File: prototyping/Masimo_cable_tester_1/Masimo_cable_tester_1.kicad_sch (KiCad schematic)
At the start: 28 parts, among them J1 Touchscreen HMI, J10 5V Jumper, J16 Debug Connections, J17 Banana Jack, J2 Conn_01x28_Socket, J3 Conn_01x28_Socket, J4 Barrel Jack 9V, J5 Conn_01x08, J6 SFML-110-02-L-D-A, J7 Conn_01x03_Pin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

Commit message: Prototype Schematic and PCB Updates
Made a few changes to the schematic for ease of tracing on the PCB design. Started PCB layout of components, no traces yet
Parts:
- J10: value 5V Jumper -> MCU Board Power
- J2: value Conn_01x28_Socket -> Curiosity Nano AVR128DB48
- J5: value Conn_01x08 -> MicroSD PinHeader
- J7: value Conn_01x03_Pin -> HMI Power Toggle
- J8: value Jumper Pins 5V -> Board Power
- J9: value VOFF Jumper -> VOFF Toggle
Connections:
- net ADC 1: now also J6.02; no longer J6.01
- net ADC 10: now also J6.20; no longer J6.10
- net ADC 2: now also J6.04; no longer J6.03
- net ADC 3: now also J6.06; no longer J6.05
- net ADC 4: now also J6.08; no longer J6.07
- net ADC 5: now also J6.10; no longer J6.09
- net ADC 6: now also J6.12; no longer J6.02
- net ADC 7: now also J6.14; no longer J6.04
- net ADC 8: now also J6.16; no longer J6.06
- net ADC 9: now also J6.18; no longer J6.08
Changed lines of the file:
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@@
 	(global_label "MP10"
 		(shape input)
-		(at 166.37 92.71 0)
+		(at 166.37 105.41 0)
 		(fields_autoplaced yes)
 		(effects
@@
 		)
 		(property "Intersheetrefs" "${INTERSHEET_REFS}"
-			(at 174.4956 92.71 0)
+			(at 174.4956 105.41 0)
 			(effects
 				(font
@@
 	(global_label "MP3"
 		(shape input)
-		(at 140.97 87.63 180)
+		(at 166.37 87.63 0)
 		(fields_autoplaced yes)
 		(effects
@@
 				(size 1.27 1.27)
 			)
-			(justify right)
+			(justify left)
 		)
 		(property "Intersheetrefs" "${INTERSHEET_REFS}"
-			(at 134.0539 87.63 0)
+			(at 173.2861 87.63 0)
 			(effects
 				(font
 					(size 1.27 1.27)
 				)
-				(justify right)
+				(justify left)
 				(hide yes)
 			)
@@
 	(global_label "MP7"
 		(shape input)
-		(at 166.37 85.09 0)
+		(at 166.37 97.79 0)
 		(fields_autoplaced yes)
 		(effects
@@
 		)
 		(property "Intersheetrefs" "${INTERSHEET_REFS}"
-			(at 173.2861 85.09 0)
+			(at 173.2861 97.79 0)
 			(effects
 				(font
@@
 	(global_label "MP4"
 		(shape input)
-		(at 140.97 90.17 180)
+		(at 166.37 90.17 0)
 		(fields_autoplaced yes)
 		(effects
@@
 				(size 1.27 1.27)
 			)
-			(justify right)
+			(justify left)
 		)
 		(property "Intersheetrefs" "${INTERSHEET_REFS}"
-			(at 134.0539 90.17 0)
+			(at 173.2861 90.17 0)
 			(effects
 				(font
 					(size 1.27 1.27)
 				)
-				(justify right)
+				(justify left)
 				(hide yes)
 			)
@@
 	(global_label "MP5"
 		(shape input)
-		(at 140.97 92.71 180)
+		(at 166.37 92.71 0)
 		(fields_autoplaced yes)
 		(effects
@@
 				(size 1.27 1.27)
 			)
-			(justify right)
+			(justify left)
 		)
 		(property "Intersheetrefs" "${INTERSHEET_REFS}"
-			(at 134.0539 92.71 0)
+			(at 173.2861 92.71 0)
 			(effects
 				(font
 					(size 1.27 1.27)
 				)
-				(justify right)
+				(justify left)
 				(hide yes)
 			)
@@
 	(global_label "MP6"
 		(shape input)
-		(at 166.37 82.55 0)
+		(at 166.37 95.25 0)
 		(fields_autoplaced yes)
 		(effects
@@
 		)
 		(property "Intersheetrefs" "${INTERSHEET_REFS}"
-			(at 173.2861 82.55 0)
+			(at 173.2861 95.25 0)
 			(effects
 				(font
@@
 	(global_label "MP2"
 		(shape input)
-		(at 140.97 85.09 180)
+		(at 166.37 85.09 0)
 		(fields_autoplaced yes)
 		(effects
@@
 				(size 1.27 1.27)
 			)
-			(justify right)
+			(justify left)
 		)
 		(property "Intersheetrefs" "${INTERSHEET_REFS}"
-			(at 134.0539 85.09 0)
+			(at 173.2861 85.09 0)
 			(effects
 				(font
 					(size 1.27 1.27)
 				)
-				(justify right)
+				(justify left)
 				(hide yes)
 			)
@@
 	(global_label "MP9"
 		(shape input)
-		(at 166.37 90.17 0)
+		(at 166.37 102.87 0)
 		(fields_autoplaced yes)
 		(effects
@@
 		)
 		(property "Intersheetrefs" "${INTERSHEET_REFS}"
-			(at 173.2861 90.17 0)
+			(at 173.2861 102.87 0)
 			(effects
 				(font
@@
 	(global_label "MP8"
 		(shape input)
-		(at 166.37 87.63 0)
+		(at 166.37 100.33 0)
 		(fields_autoplaced yes)
 		(effects
@@
 		)
 		(property "Intersheetrefs" "${INTERSHEET_REFS}"
-			(at 173.2861 87.63 0)
+			(at 173.2861 100.33 0)
 			(effects
 				(font
@@
 	(global_label "MP1"
 		(shape input)
-		(at 140.97 82.55 180)
+		(at 166.37 82.55 0)
 		(fields_autoplaced yes)
 		(effects
@@
 				(size 1.27 1.27)
 			)
-			(justify right)
+			(justify left)
 		)
 		(property "Intersheetrefs" "${INTERSHEET_REFS}"
-			(at 134.0539 82.55 0)
+			(at 173.2861 82.55 0)
 			(effects
 				(font
 					(size 1.27 1.27)
 				)
-				(justify right)
+				(justify left)
 				(hide yes)
 			)
@@
 		(dnp no)
 		(property "Reference" "C2"
-			(at 93.98 43.1799 0)
+			(at 90.678 42.418 0)
 			(effects
 				(font
@@
 				)
 				(justify left)
-				(hide yes)
 			)
 		)
@@
 		(on_board yes)
 		(dnp no)
-		(fields_autoplaced yes)
 		(property "Reference" "J8"
 			(at 102.87 34.9249 90)
@@
 			)
 		)
-		(property "Value" "Jumper Pins 5V"
-			(at 102.87 37.4649 90)
+		(property "Value" "Board Power"
+			(at 94.488 33.782 90)
 			(effects
 				(font
@@
 		(dnp no)
 		(property "Reference" "C1"
-			(at 67.31 43.1799 0)
+			(at 70.866 42.164 0)
 			(effects
 				(font
@@
 				)
 				(justify left)
-				(hide yes)
 			)
 		)
@@
 			)
 		)
-		(property "Value" "Conn_01x08"
+		(property "Value" "MicroSD PinHeader"
 			(at 139.7 33.02 0)
 			(effects
@@
 		(on_board yes)
 		(dnp no)
-		(fields_autoplaced yes)
 		(property "Reference" "J9"
 			(at 91.44 114.9349 90)
@@
 			)
 		)
-		(property "Value" "VOFF Jumper"
-			(at 91.44 117.4749 90)
+		(property "Value" "VOFF Toggle"
+			(at 83.566 113.792 90)
 			(effects
 				(font
@@
 			)
 		)
-		(property "Value" "Conn_01x03_Pin"
+		(property "Value" "HMI Power Toggle"
 			(at 78.74 86.3599 0)
 			(effects
@@
 		(on_board yes)
 		(dnp no)
-		(fields_autoplaced yes)
 		(property "Reference" "J10"
 			(at 86.36 136.5251 90)
@@
 			)
 		)
-		(property "Value" "5V Jumper"
-			(at 91.44 135.2549 90)
+		(property "Value" "MCU Board Power"
+			(at 81.026 137.668 90)
 			(effects
 				(font
@@
 			)
 		)
-		(property "Value" "Conn_01x28_Socket"
+		(property "Value" "Curiosity Nano AVR128DB48"
 			(at 49.53 153.6699 0)
 			(effects

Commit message: Layed traces down.
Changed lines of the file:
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@@
 (kicad_sch
-	(version 20231120)
+	(version 20250114)
 	(generator "eeschema")
-	(generator_version "8.0")
+	(generator_version "9.0")
 	(paper "A")
 	(title_block
@@
 		(comment 1 "Designed for use with the AVR128DB48 Curiosity Nano")
 	)
+	(rectangle
+		(start 19.05 24.765)
+		(end 121.285 60.325)
+		(stroke
+			(width 0)
+			(type default)
+		)
+		(fill
+			(type none)
+		)
+	)
+	(rectangle
+		(start 193.04 45.085)
+		(end 255.905 154.305)
+		(stroke
+			(width 0)
+			(type default)
+		)
+		(fill
+			(type none)
+		)
+	)
+	(text "Signal Relay"
+		(exclude_from_sim no)
+		(at 146.05 129.286 0)
+		(effects
+			(font
+				(size 2.032 2.032)
+				(thickness 0.4064)
+				(bold yes)
+			)
+		)
+	)
+	(text "MicroSD"
+		(exclude_from_sim no)
+		(at 144.272 26.924 0)
+		(effects
+			(font
+				(size 2.032 2.032)
+				(thickness 0.4064)
+				(bold yes)
+			)
+		)
+	)
+	(text "20-Pin Connector"
+		(exclude_from_sim no)
+		(at 153.416 73.914 0)
+		(effects
+			(font
+				(size 2.032 2.032)
+				(thickness 0.4064)
+				(bold yes)
+			)
+		)
+	)
+	(text "Power"
+		(exclude_from_sim no)
+		(at 65.024 30.226 0)
+		(effects
+			(font
+				(size 2.032 2.032)
+				(thickness 0.4064)
+				(bold yes)
+			)
+		)
+	)
+	(text "AVR128DB48\nMicrocontroller"
+		(exclude_from_sim no)
+		(at 54.356 109.22 0)
+		(effects
+			(font
+				(size 2.54 2.54)
+				(thickness 0.508)
+				(bold yes)
+			)
+		)
+	)
+	(text "Analog IF"
+		(exclude_from_sim no)
+		(at 225.044 49.276 0)
+		(effects
+			(font
+				(size 2.032 2.032)
+				(thickness 0.4064)
+				(bold yes)
+			)
+		)
+	)
 	(junction
 		(at 227.33 69.85)
@@
 		)
 	)
-	(rectangle
-		(start 19.05 24.765)
-		(end 121.285 60.325)
-		(stroke
-			(width 0)
-			(type default)
-		)
-		(fill
-			(type none)
-		)
-	)
-	(rectangle
-		(start 193.04 45.085)
-		(end 255.905 154.305)
-		(stroke
-			(width 0)
-			(type default)
-		)
-		(fill
-			(type none)
-		)
-	)
-	(text "Signal Relay"
-		(exclude_from_sim no)
-		(at 146.05 129.286 0)
-		(effects
-			(font
-				(size 2.032 2.032)
-				(thickness 0.4064)
-				(bold yes)
-			)
-		)
-	)
-	(text "MicroSD"
-		(exclude_from_sim no)
-		(at 144.272 26.924 0)
-		(effects
-			(font
-				(size 2.032 2.032)
-				(thickness 0.4064)
-				(bold yes)
-			)
-		)
-	)
-	(text "20-Pin Connector"
-		(exclude_from_sim no)
-		(at 153.416 73.914 0)
-		(effects
-			(font
-				(size 2.032 2.032)
-				(thickness 0.4064)
-				(bold yes)
-			)
-		)
-	)
-	(text "Power"
-		(exclude_from_sim no)
-		(at 65.024 30.226 0)
-		(effects
-			(font
-				(size 2.032 2.032)
-				(thickness 0.4064)
-				(bold yes)
-			)
-		)
-	)
-	(text "AVR128DB48\nMicrocontroller"
-		(exclude_from_sim no)
-		(at 54.356 109.22 0)
-		(effects
-			(font
-				(size 2.54 2.54)
-				(thickness 0.508)
-				(bold yes)
-			)
-		)
-	)
-	(text "Analog IF"
-		(exclude_from_sim no)
-		(at 225.044 49.276 0)
-		(effects
-			(font
-				(size 2.032 2.032)
-				(thickness 0.4064)
-				(bold yes)
-			)
-		)
-	)
 	(global_label "5V"
 		(shape input)
@@
 		)
 	)
+	(embedded_fonts no)
 )

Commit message: PCB Update
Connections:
- net ADC 1: now also J3.12 (Pin_12); no longer J3.22 (Pin_22)
- net ADC 10: now also J3.22 (Pin_22); no longer J3.10 (Pin_10)
- net ADC 2: now also J3.13 (Pin_13); no longer J3.21 (Pin_21)
- net ADC 3: now also J3.15 (Pin_15); no longer J3.20 (Pin_20)
- net ADC 4: now also J3.16 (Pin_16); no longer J3.19 (Pin_19)
- net ADC 5: now also J3.17 (Pin_17); no longer J3.18 (Pin_18)
- net ADC 6: now also J3.18 (Pin_18); no longer J3.17 (Pin_17)
- net ADC 7: now also J3.19 (Pin_19); no longer J3.16 (Pin_16)
- net ADC 8: now also J3.20 (Pin_20); no longer J3.15 (Pin_15)
- net ADC 9: now also J3.21 (Pin_21); no longer J3.11 (Pin_11)
- net BJ1: no longer J17.2 (Pin_2)
- net BJ2: now also J17.2 (Pin_2)
- net CD: now also J2.9 (Pin_9); no longer J3.13 (Pin_13)
- net CS: now also J2.10 (Pin_10); no longer J3.12 (Pin_12)
- net CTRL 1: now also J3.11 (Pin_11); no longer J3.9 (Pin_9)
- net CTRL 10: now also J2.22 (Pin_22); no longer J2.18 (Pin_18)
- net CTRL 2: now also J3.10 (Pin_10); no longer J3.8 (Pin_8)
- net CTRL 3: now also J3.9 (Pin_9); no longer J3.7 (Pin_7)
- net CTRL 4: now also J3.8 (Pin_8); no longer J3.6 (Pin_6)
- net CTRL 5: now also J3.7 (Pin_7); no longer J2.23 (Pin_23)
- net CTRL 6: now also J3.6 (Pin_6); no longer J2.22 (Pin_22)
- net CTRL 7: now also J3.4 (Pin_4); no longer J2.21 (Pin_21)
- net CTRL 8: now also J3.3 (Pin_3); no longer J2.20 (Pin_20)
- net CTRL 9: now also J2.21 (Pin_21); no longer J2.19 (Pin_19)
- net RSig: now also J2.23 (Pin_23); no longer J3.4 (Pin_4)

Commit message: Revert "Test push."
This reverts commit 5521fc2d8bd7614dad4a2481f5d65b20cf141a6d, reversing
changes made to 7098e4d101a90ac0b58b20fb139d108fe580d24d.
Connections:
- net ADC 1: now also J3.22 (Pin_22); no longer J3.12 (Pin_12)
- net ADC 10: now also J3.10 (Pin_10); no longer J3.22 (Pin_22)
- net ADC 2: now also J3.21 (Pin_21); no longer J3.13 (Pin_13)
- net ADC 3: now also J3.20 (Pin_20); no longer J3.15 (Pin_15)
- net ADC 4: now also J3.19 (Pin_19); no longer J3.16 (Pin_16)
- net ADC 5: now also J3.18 (Pin_18); no longer J3.17 (Pin_17)
- net ADC 6: now also J3.17 (Pin_17); no longer J3.18 (Pin_18)
- net ADC 7: now also J3.16 (Pin_16); no longer J3.19 (Pin_19)
- net ADC 8: now also J3.15 (Pin_15); no longer J3.20 (Pin_20)
- net ADC 9: now also J3.11 (Pin_11); no longer J3.21 (Pin_21)
- net BJ1: now also J17.2 (Pin_2)
- net BJ2: no longer J17.2 (Pin_2)
- net CD: now also J3.13 (Pin_13); no longer J2.9 (Pin_9)
- net CS: now also J3.12 (Pin_12); no longer J2.10 (Pin_10)
- net CTRL 1: now also J3.9 (Pin_9); no longer J3.11 (Pin_11)
- net CTRL 10: now also J2.18 (Pin_18); no longer J2.22 (Pin_22)
- net CTRL 2: now also J3.8 (Pin_8); no longer J3.10 (Pin_10)
- net CTRL 3: now also J3.7 (Pin_7); no longer J3.9 (Pin_9)
- net CTRL 4: now also J3.6 (Pin_6); no longer J3.8 (Pin_8)
- net CTRL 5: now also J2.23 (Pin_23); no longer J3.7 (Pin_7)
- net CTRL 6: now also J2.22 (Pin_22); no longer J3.6 (Pin_6)
- net CTRL 7: now also J2.21 (Pin_21); no longer J3.4 (Pin_4)
- net CTRL 8: now also J2.20 (Pin_20); no longer J3.3 (Pin_3)
- net CTRL 9: now also J2.19 (Pin_19); no longer J2.21 (Pin_21)
- net RSig: now also J3.4 (Pin_4); no longer J2.23 (Pin_23)

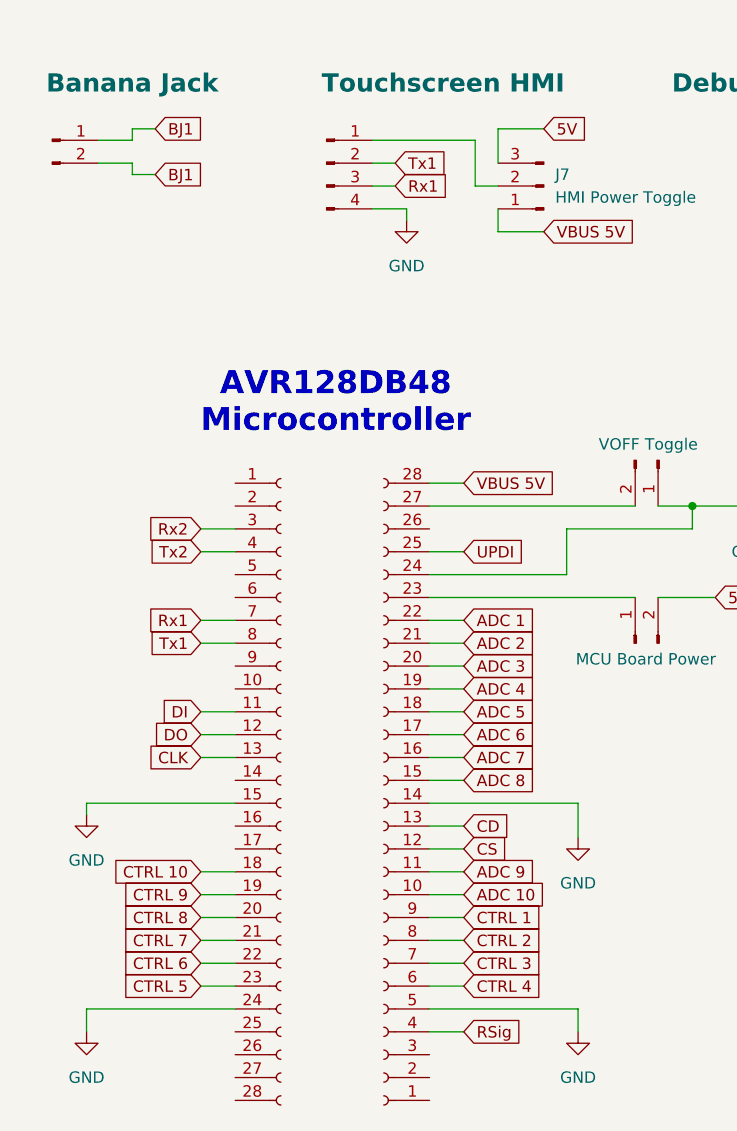
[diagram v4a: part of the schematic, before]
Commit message: Prototype Schematic and PCB Update
Updated the prototype schematic and PCB. Put all analog if tags on 1 side for easier PCB tracing. By doing this I also changed the location of the Rsig, CD, and CS locations on the MC.
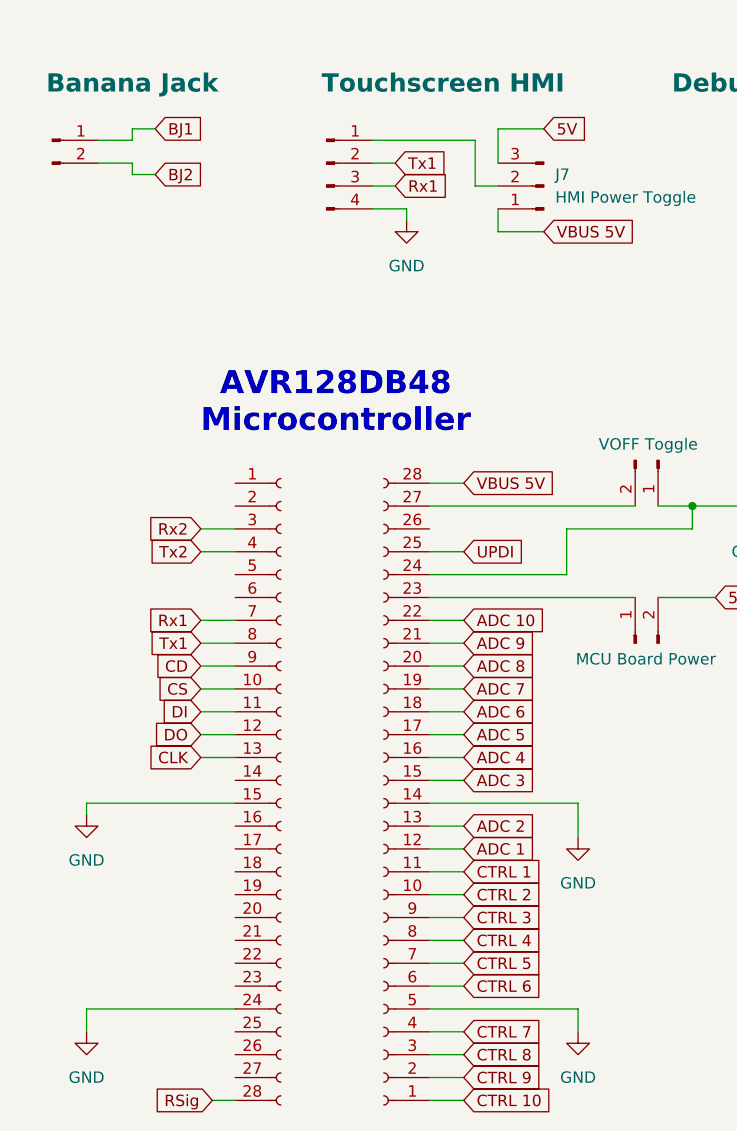
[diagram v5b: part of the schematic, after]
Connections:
- net ADC 1: now also J3.12 (Pin_12); no longer J3.22 (Pin_22)
- net ADC 10: now also J3.22 (Pin_22); no longer J3.10 (Pin_10)
- net ADC 2: now also J3.13 (Pin_13); no longer J3.21 (Pin_21)
- net ADC 3: now also J3.15 (Pin_15); no longer J3.20 (Pin_20)
- net ADC 4: now also J3.16 (Pin_16); no longer J3.19 (Pin_19)
- net ADC 5: now also J3.17 (Pin_17); no longer J3.18 (Pin_18)
- net ADC 6: now also J3.18 (Pin_18); no longer J3.17 (Pin_17)
- net ADC 7: now also J3.19 (Pin_19); no longer J3.16 (Pin_16)
- net ADC 8: now also J3.20 (Pin_20); no longer J3.15 (Pin_15)
- net ADC 9: now also J3.21 (Pin_21); no longer J3.11 (Pin_11)
- net BJ1: no longer J17.2 (Pin_2)
- net BJ2: now also J17.2 (Pin_2)
- net CD: now also J2.9 (Pin_9); no longer J3.13 (Pin_13)
- net CS: now also J2.10 (Pin_10); no longer J3.12 (Pin_12)
- net CTRL 1: now also J3.11 (Pin_11); no longer J3.9 (Pin_9)
- net CTRL 10: now also J3.1 (Pin_1); no longer J2.18 (Pin_18)
- net CTRL 2: now also J3.10 (Pin_10); no longer J3.8 (Pin_8)
- net CTRL 3: now also J3.9 (Pin_9); no longer J3.7 (Pin_7)
- net CTRL 4: now also J3.8 (Pin_8); no longer J3.6 (Pin_6)
- net CTRL 5: now also J3.7 (Pin_7); no longer J2.23 (Pin_23)
- net CTRL 6: now also J3.6 (Pin_6); no longer J2.22 (Pin_22)
- net CTRL 7: now also J3.4 (Pin_4); no longer J2.21 (Pin_21)
- net CTRL 8: now also J3.3 (Pin_3); no longer J2.20 (Pin_20)
- net CTRL 9: now also J3.2 (Pin_2); no longer J2.19 (Pin_19)
- net RSig: now also J2.28 (Pin_28); no longer J3.4 (Pin_4)

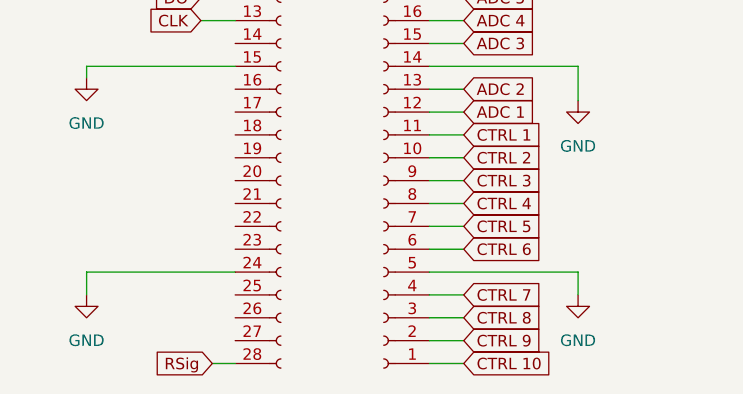
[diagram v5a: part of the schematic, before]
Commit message: Prototype PCB Changes
A few routing changes to the Prototype PCB.
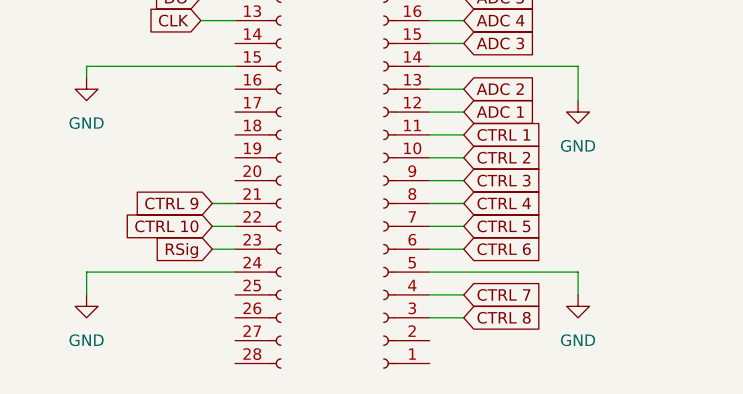
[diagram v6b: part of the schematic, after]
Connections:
- net CTRL 10: now also J2.22 (Pin_22); no longer J3.1 (Pin_1)
- net CTRL 9: now also J2.21 (Pin_21); no longer J3.2 (Pin_2)
- net RSig: now also J2.23 (Pin_23); no longer J2.28 (Pin_28)
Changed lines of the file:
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@@
+	(wire
+		(pts
+			(xy 40.64 168.91) (xy 43.18 168.91)
+		)
+		(stroke
+			(width 0)
+			(type default)
+		)
+	)
 	(wire
 		(pts
@@
 	(wire
 		(pts
+			(xy 40.64 171.45) (xy 43.18 171.45)
+		)
+		(stroke
+			(width 0)
+			(type default)
+		)
+	)
+	(wire
+		(pts
 			(xy 214.63 55.88) (xy 227.33 55.88)
 		)
@@
 	(wire
 		(pts
-			(xy 64.77 186.69) (xy 68.58 186.69)
-		)
-		(stroke
-			(width 0)
-			(type default)
-		)
-	)
-	(wire
-		(pts
 			(xy 64.77 156.21) (xy 68.58 156.21)
 		)
@@
 	(wire
 		(pts
+			(xy 40.64 173.99) (xy 43.18 173.99)
+		)
+		(stroke
+			(width 0)
+			(type default)
+		)
+	)
+	(wire
+		(pts
 			(xy 46.99 43.18) (xy 41.91 43.18)
 		)
@@
 	(wire
 		(pts
-			(xy 64.77 184.15) (xy 68.58 184.15)
-		)
-		(stroke
-			(width 0)
-			(type default)
-		)
-	)
-	(wire
-		(pts
 			(xy 144.78 54.61) (xy 146.05 54.61)
 		)
@@
 	(wire
 		(pts
-			(xy 40.64 186.69) (xy 43.18 186.69)
-		)
-		(stroke
-			(width 0)
-			(type default)
-		)
-	)
-	(wire
-		(pts
 			(xy 64.77 125.73) (xy 68.58 125.73)
 		)
@@
 	(global_label "CTRL 10"
 		(shape input)
-		(at 68.58 186.69 0)
-		(fields_autoplaced yes)
-		(effects
-			(font
-				(size 1.27 1.27)
-			)
-			(justify left)
-		)
-		(property "Intersheetrefs" "${INTERSHEET_REFS}"
-			(at 79.4875 186.69 0)
-			(effects
-				(font
-					(size 1.27 1.27)
-				)
-				(justify left)
+		(at 40.64 171.45 180)
+		(fields_autoplaced yes)
+		(effects
+			(font
+				(size 1.27 1.27)
+			)
+			(justify right)
+		)
+		(property "Intersheetrefs" "${INTERSHEET_REFS}"
+			(at 29.7325 171.45 0)
+			(effects
+				(font
+					(size 1.27 1.27)
+				)
+				(justify right)
 				(hide yes)
 			)
@@
 	(global_label "RSig"
 		(shape input)
-		(at 40.64 186.69 180)
+		(at 40.64 173.99 180)
 		(fields_autoplaced yes)
 		(effects
@@
 		)
 		(property "Intersheetrefs" "${INTERSHEET_REFS}"
-			(at 33.4215 186.69 0)
+			(at 33.4215 173.99 0)
 			(effects
 				(font
@@
 	(global_label "CTRL 9"
 		(shape input)
-		(at 68.58 184.15 0)
-		(fields_autoplaced yes)
-		(effects
-			(font
-				(size 1.27 1.27)
-			)
-			(justify left)
-		)
-		(property "Intersheetrefs" "${INTERSHEET_REFS}"
-			(at 78.278 184.15 0)
-			(effects
-				(font
-					(size 1.27 1.27)
-				)
-				(justify left)
-				(hide yes)
-			)
+		(at 40.64 168.91 180)
+		(fields_autoplaced yes)
+		(effects
+			(font
+				(size 1.27 1.27)
+			)
+			(justify right)
+		)
+		(property "Intersheetrefs" "${INTERSHEET_REFS}"
+			(at 30.942 168.91 0)
+			(effects
+				(font
+					(size 1.27 1.27)
+				)
+				(justify right)
+				(hide yes)
+			)
